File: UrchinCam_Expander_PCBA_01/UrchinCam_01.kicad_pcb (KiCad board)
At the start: 4 copper layers, 31.5 x 65 mm, 90 parts, among them J1 95157-440LF, J2 SM04B-GHS, J3 SM04B-GHS, J4 SM02B-GHS, J5 SM04B-GHS, U1 MP6550, U2 ADS1115IDGS, U3 BNO085, U4 TSR3-2450N, U5 RTL8152B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

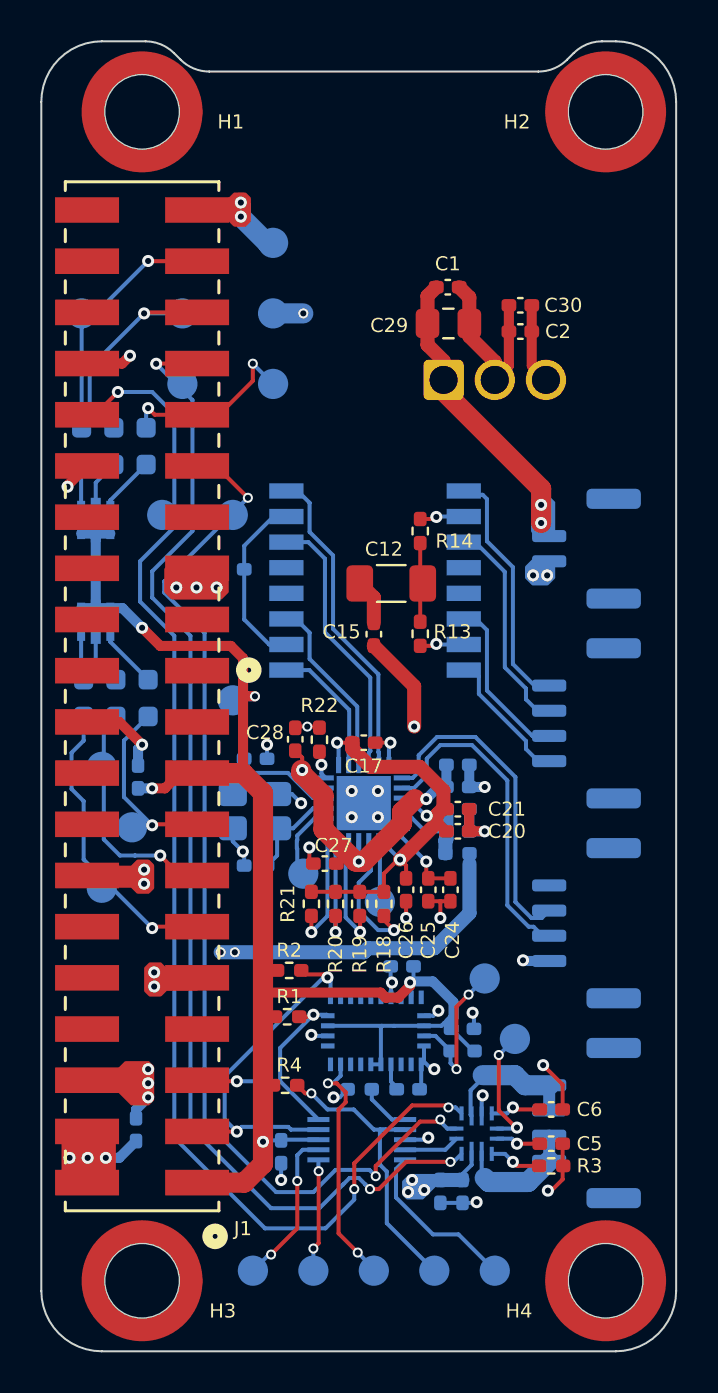
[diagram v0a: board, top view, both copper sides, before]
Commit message: Fixing ethernet routing.
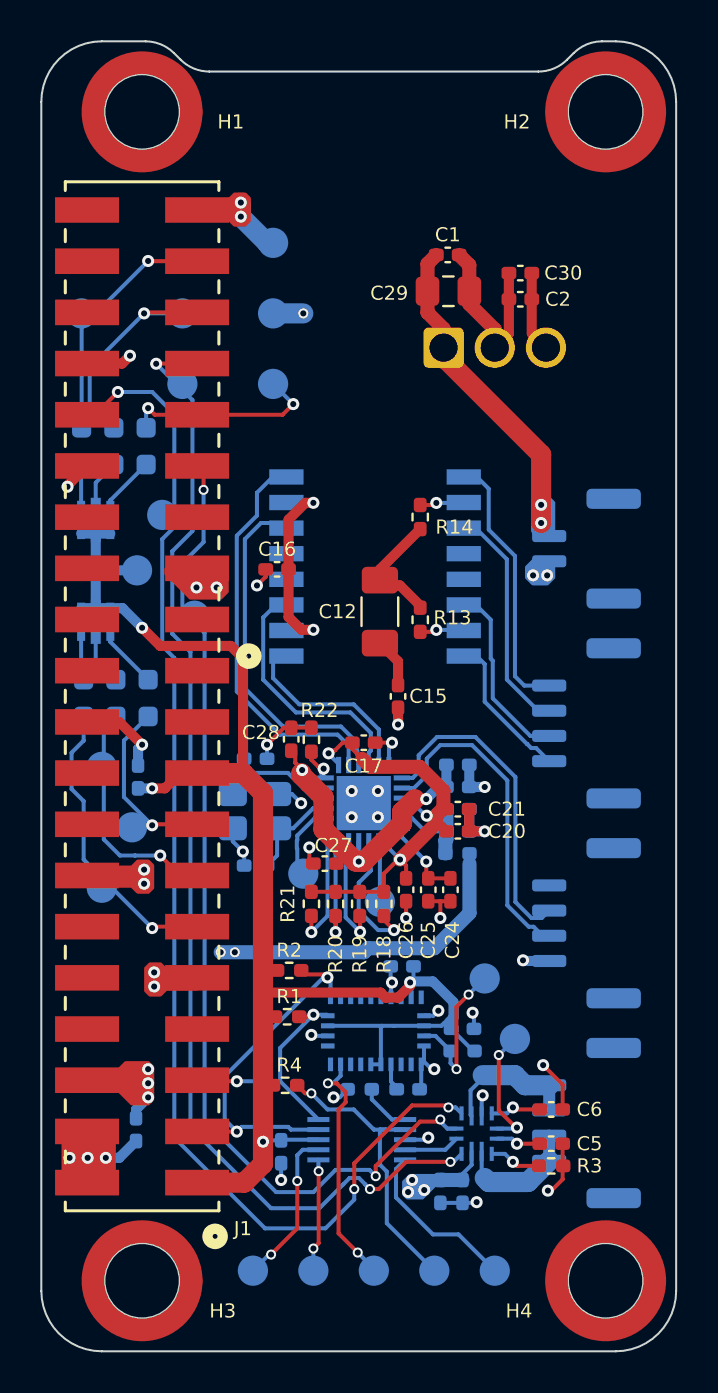
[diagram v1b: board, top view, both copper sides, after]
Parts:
- C16: moved to F.Cu
- moved TP3 8.01 mm to (139.8, 96.8)
- moved TP16 5.35 mm to (142.6, 99.0)
- moved C15 3.31 mm to (152.7, 103.0)
- moved C16 2.20 mm to (146.7, 96.7)
- moved C1 1.60 mm to (155.2, 81.1)
- moved C2 1.60 mm to (158.8, 83.3)
- moved C29 1.60 mm to (155.2, 82.9)
- moved C30 1.60 mm to (158.8, 82.0)
- moved U4 1.60 mm to (155.0, 85.7)
- moved C12 1.51 mm to (151.8, 98.8), turned to -90 degrees
- moved U6 0.70 mm to (147.2, 101.0)
- moved R13 0.69 mm to (153.8, 99.2)
- moved R14 0.69 mm to (153.8, 94.1)
- moved R22 0.40 mm to (148.4, 105.2)
- moved C28 0.20 mm to (147.4, 105.1)
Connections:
- J2 pad 1: /R- -> /T+
- J2 pad 2: /R+ -> /T-
- J2 pad 3: /T- -> /R+
- J2 pad 4: /T+ -> /R-
- U6 pad 1: /MDI0_P -> /MDI1_N
- U6 pad 11: /R+ -> /T-
- U6 pad 14: /T- -> /R+
- U6 pad 16: /T+ -> /R-
- U6 pad 3: /MDI0_N -> /MDI1_P
- U6 pad 6: /MDI1_P -> /MDI0_N
- U6 pad 8: /MDI1_N -> /MDI0_P
- U6 pad 9: /R- -> /T+
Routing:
- net /MDI0_P: track 6.68 -> 19.7 mm
- net /MDI0_N: track 9.01 -> 17.7 mm
- net /T+: track 6.85 -> 13.2 mm
- net /MDI1_N: track 15.8 -> 9.82 mm
- net /R-: track 12.4 -> 7.49 mm
- net /PI_GPIO5: track 52.9 -> 49.8 mm
- net /T-: track 8.40 -> 11.5 mm
- net GND: track 63.8 -> 61.4 mm, vias 45 -> 44
- net Net-(J4-Pin_1): track 14.6 -> 16.7 mm
- net Net-(C12-Pad1): track 4.01 -> 5.99 mm
- net Net-(C16-Pad1): track 8.96 -> 10.6 mm, vias 0 -> 2
- net /R+: track 10.8 -> 9.16 mm
- net /PI_GPIO12: track 62.4 -> 61.5 mm
- net /MDI1_P: track 13.5 -> 12.6 mm
- net /PI_GPIO13: track 59.0 -> 58.1 mm
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
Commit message: Fixing via diameters.
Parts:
- added G***: LOGO, LOGO, F.Cu at (152.5, 127.2)
- added G***: LOGO, LOGO, B.Cu at (151.6, 75.9)
- H1, H2, H3, H4: value 9774050151R -> M2.5; footprint Mounting_Wuerth:Mounting_Wuerth_WA-SMSI-M2.5_H5mm_9774050151R -> Mounting_Holes:M2.5_Mounting_Hole_2.9mm_unplated
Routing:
- net Net-(U2-AIN2): track 5.61 -> 6.73 mm
- net /IMU_INT: track 12.1 -> 13.0 mm
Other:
- board text added: "UrchinCam v0.1 2026"

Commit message: Adding DCDC model.
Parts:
- U4: value TSR3-2450N -> TSR 3-2450N; footprint Converter_DCDC:Converter_DCDC_TRACO_TSR2-24xxN_TSR2-24xxxN_THT -> DCDC_Converters:Traco_TSR 3-2450N
- moved U4 2.54 mm to (157.5, 85.7)
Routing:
- net +5V: track 112.5 -> 114.5 mm
